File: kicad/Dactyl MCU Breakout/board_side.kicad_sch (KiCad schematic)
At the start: 19 parts, among them J1 Columns, J2 Rows, J3 Thumbs, J4 Display, J5 Split, J6 Extrernal, J7 JST, SW1 Reset, SW2 Battery, SW3 LED, U1 Nice!Nano/2040, U2 74HC595

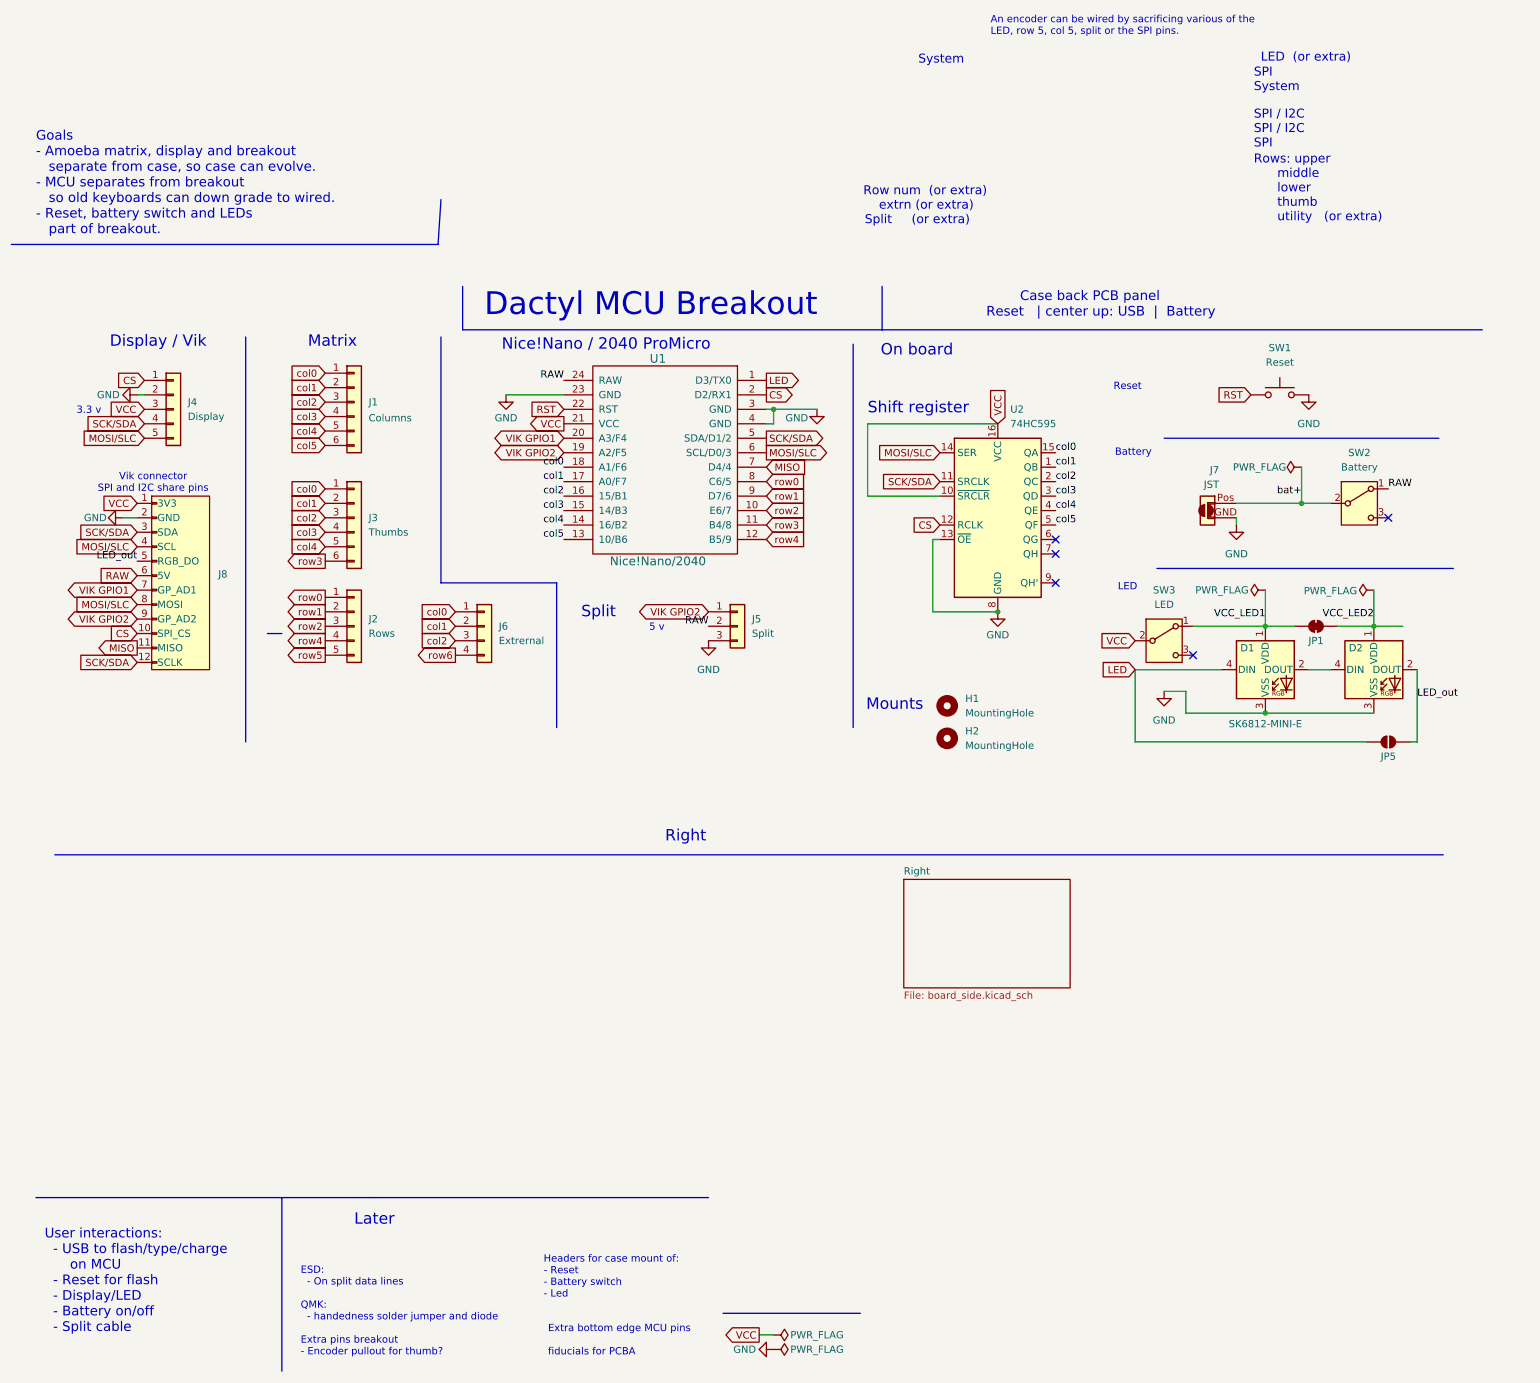
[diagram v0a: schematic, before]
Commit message: refactor: board half sub sheet, some net labels
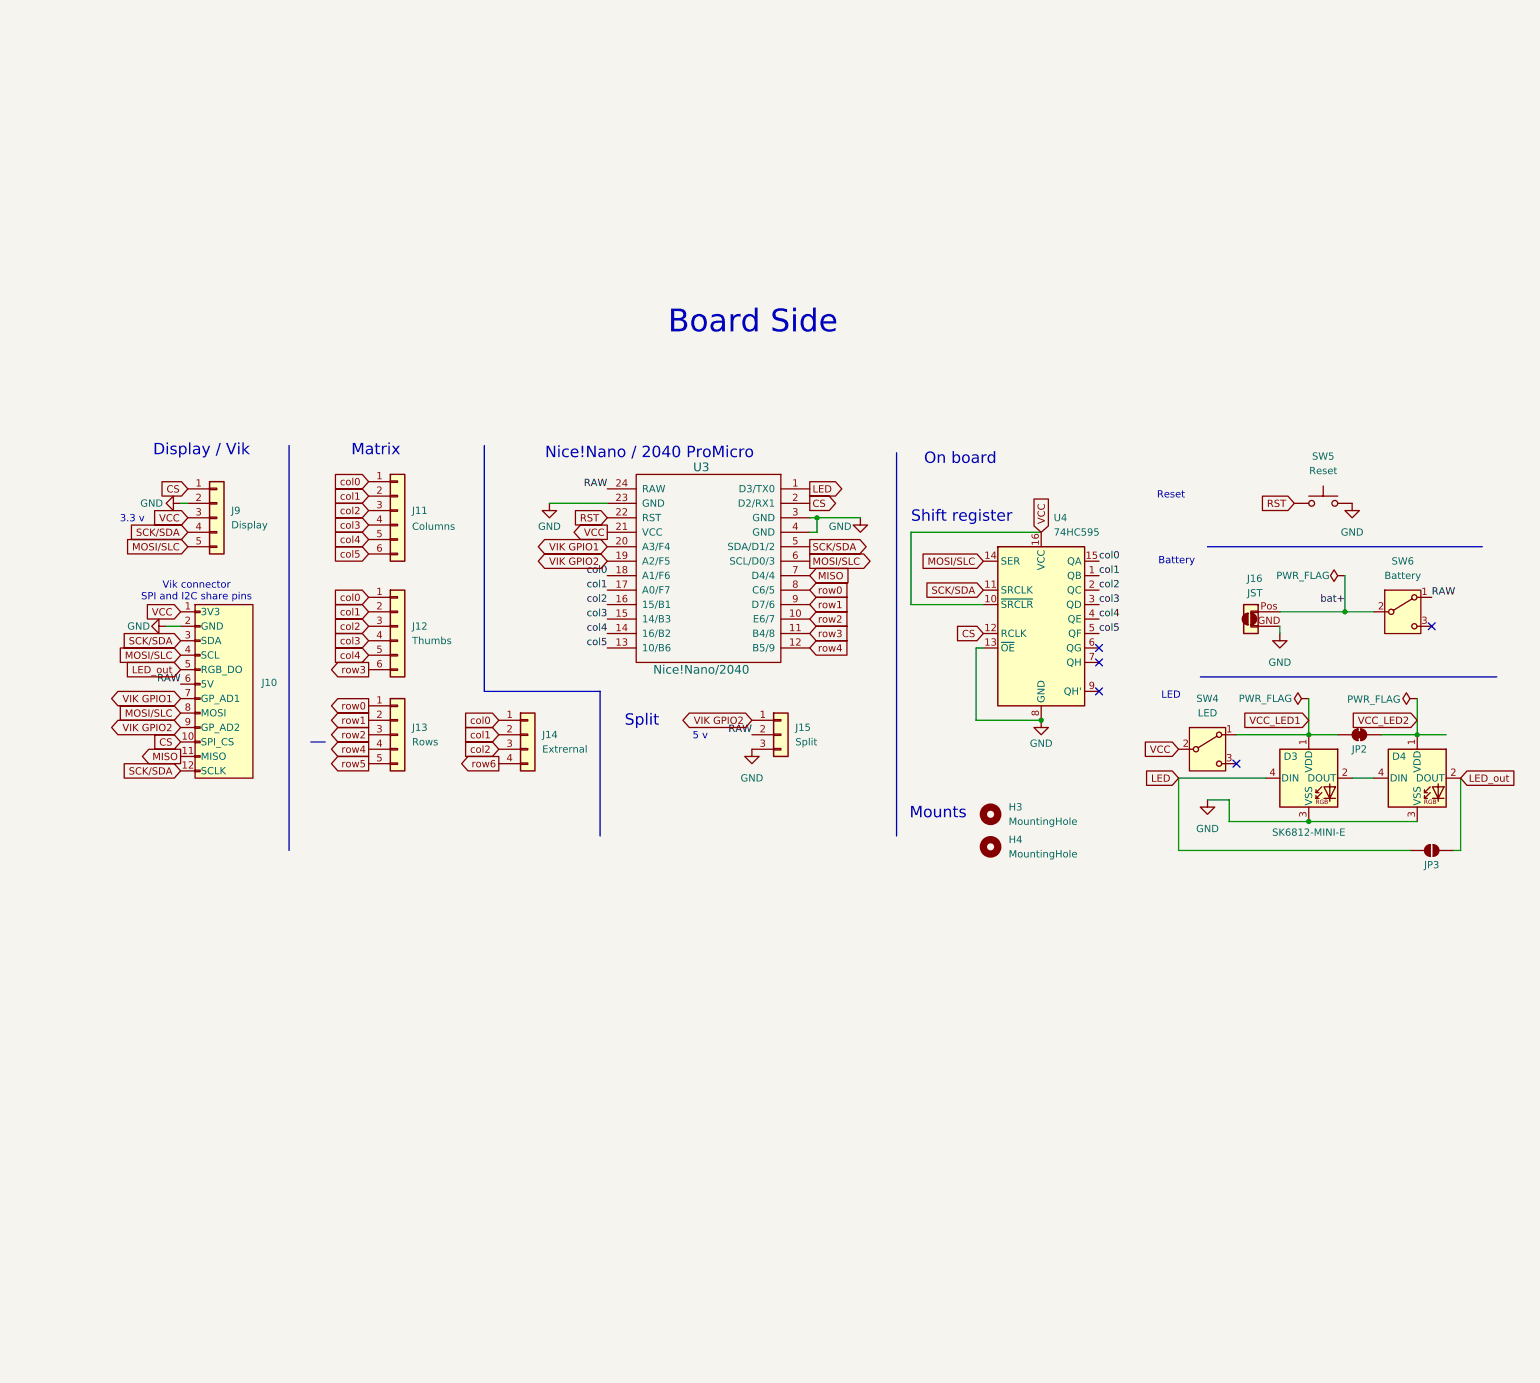
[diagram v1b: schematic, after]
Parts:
- removed D1, D2: SK6812-MINI-E, Dactyl:SK6812-MINI-E-Dog2, symbol Dactyl:SK6812-MINI-E
- removed H1, H2: MountingHole, MountingHole:MountingHole_3.2mm_M3_DIN965_Pad, symbol Mechanical:MountingHole
- removed J1: Columns, Connector_PinHeader_2.54mm:PinHeader_1x06_P2.54mm_Vertical, symbol Connector_Generic:Conn_01x06
- removed J2: Rows, Connector_PinHeader_2.54mm:PinHeader_1x05_P2.54mm_Vertical, symbol Connector_Generic:Conn_01x05
- removed J3: Thumbs, Connector_PinHeader_2.54mm:PinHeader_1x06_P2.54mm_Vertical, symbol Connector_Generic:Conn_01x06
- removed J4: Display, Connector_PinHeader_2.54mm:PinHeader_1x05_P2.54mm_Vertical, symbol Connector_Generic:Conn_01x05
- removed J5: Split, Connector_PinHeader_2.54mm:PinHeader_1x03_P2.54mm_Vertical, symbol Connector_Generic:Conn_01x03
- removed J6: Extrernal, Connector_PinHeader_2.54mm:PinHeader_1x04_P2.54mm_Vertical, symbol Connector_Generic:Conn_01x04
- removed J7: JST, Dactyl:JST_PH_S2B-PH-K_1x02_P2.00mm_Horizontal, symbol Dactyl:Conn_01x02_Jump_Two_Side
- removed J8: ~, symbol Dactyl:vik-keyboard-connector
- removed JP1: LED2 cutoff, Jumper:SolderJumper-2_P1.3mm_Bridged_RoundedPad1.0x1.5mm, symbol Jumper:SolderJumper_2_Bridged
- removed JP5: LED2 cutoff, Jumper:SolderJumper-2_P1.3mm_Bridged_RoundedPad1.0x1.5mm, symbol Jumper:SolderJumper_2_Open
- removed SW1: Reset, Dactyl:SW_Tactile_SKHL_Angled, symbol Switch:SW_Push
- removed SW2: Battery, Dactyl:SW_SPDT_JS202011AQN_wider, symbol Switch:SW_SPDT
- removed SW3: LED, Dactyl:SW_SPDT_JS202011AQN_wider, symbol Switch:SW_SPDT
- removed U1: Nice!Nano/2040, Dactyl:ProMicro_unrouted, symbol Dactyl:ProMicro_r
- removed U2: 74HC595, symbol 74xx:74HC595
- added D3, D4: SK6812-MINI-E, Dactyl:SK6812-MINI-E-Dog2, symbol Dactyl:SK6812-MINI-E
- added H3, H4: MountingHole, MountingHole:MountingHole_3.2mm_M3_DIN965_Pad, symbol Mechanical:MountingHole
- added J10: ~, symbol Dactyl:vik-keyboard-connector
- added J11: Columns, Connector_PinHeader_2.54mm:PinHeader_1x06_P2.54mm_Vertical, symbol Connector_Generic:Conn_01x06
- added J12: Thumbs, Connector_PinHeader_2.54mm:PinHeader_1x06_P2.54mm_Vertical, symbol Connector_Generic:Conn_01x06
- added J13: Rows, Connector_PinHeader_2.54mm:PinHeader_1x05_P2.54mm_Vertical, symbol Connector_Generic:Conn_01x05
- added J14: Extrernal, Connector_PinHeader_2.54mm:PinHeader_1x04_P2.54mm_Vertical, symbol Connector_Generic:Conn_01x04
- added J15: Split, Connector_PinHeader_2.54mm:PinHeader_1x03_P2.54mm_Vertical, symbol Connector_Generic:Conn_01x03
- added J16: JST, Dactyl:JST_PH_S2B-PH-K_1x02_P2.00mm_Horizontal, symbol Dactyl:Conn_01x02_Jump_Two_Side
- added J9: Display, Connector_PinHeader_2.54mm:PinHeader_1x05_P2.54mm_Vertical, symbol Connector_Generic:Conn_01x05
- added JP2: LED2 cutoff, Jumper:SolderJumper-2_P1.3mm_Bridged_RoundedPad1.0x1.5mm, symbol Jumper:SolderJumper_2_Bridged
- added JP3: LED2 cutoff, Jumper:SolderJumper-2_P1.3mm_Bridged_RoundedPad1.0x1.5mm, symbol Jumper:SolderJumper_2_Open
- added SW4: LED, Dactyl:SW_SPDT_JS202011AQN_wider, symbol Switch:SW_SPDT
- added SW5: Reset, Dactyl:SW_Tactile_SKHL_Angled, symbol Switch:SW_Push
- added SW6: Battery, Dactyl:SW_SPDT_JS202011AQN_wider, symbol Switch:SW_SPDT
- added U3: Nice!Nano/2040, Dactyl:ProMicro_unrouted, symbol Dactyl:ProMicro_r
- added U4: 74HC595, symbol 74xx:74HC595
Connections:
- net CS: now also J10.10 (SPI_CS), J9.1 (Pin_1), U3.2 (D2/RX1), U4.12 (RCLK)
- net GND: now also D3.3 (VSS), D4.3 (VSS), J10.2 (GND), J15.3 (Pin_3), J16.GND, J9.2 (Pin_2), SW5.2, U3.23 (GND), U3.3 (GND), U3.4 (GND), U4.13 (~{OE}), U4.8 (GND)
- net LED: now also D3.4 (DIN), JP3.1 (A), U3.1 (D3/TX0)
- net LED_out: now also D4.2 (DOUT), J10.5 (RGB_DO), JP3.2 (B)
- net MISO: now also J10.11 (MISO), U3.7 (D4/4)
- net MOSI/SLC: now also J10.4 (SCL), J10.8 (MOSI), J9.5 (Pin_5), U3.6 (SCL/D0/3), U4.14 (SER)
- net RAW: now also J10.6 (5V), J15.2 (Pin_2), SW6.1 (A), U3.24 (RAW)
- net RST: now also SW5.1, U3.22 (RST)
- net SCK/SDA: now also J10.12 (SCLK), J10.3 (SDA), J9.4 (Pin_4), U3.5 (SDA/D1/2), U4.11 (SRCLK)
- net VCC: now also J10.1 (3V3), J9.3 (Pin_3), SW4.2 (B), U3.21 (VCC), U4.10 (~{SRCLR}), U4.16 (VCC)
- net VCC_LED1: now also D3.1 (VDD), JP2.1 (A), SW4.1 (A)
- net VCC_LED2: now also D4.1 (VDD), JP2.2 (B)
- net VIK GPIO1: now also J10.7 (GP_AD1), U3.20 (A3/F4)
- net VIK GPIO2: now also J10.9 (GP_AD2), J15.1 (Pin_1), U3.19 (A2/F5)
- net bat+: now also J16.Pos, SW6.2 (B)
- net col0: now also J11.1 (Pin_1), J12.1 (Pin_1), J14.1 (Pin_1), U3.18 (A1/F6), U4.15 (QA)
- net col1: now also J11.2 (Pin_2), J12.2 (Pin_2), J14.2 (Pin_2), U3.17 (A0/F7), U4.1 (QB)
- net col2: now also J11.3 (Pin_3), J12.3 (Pin_3), J14.3 (Pin_3), U3.16 (15/B1), U4.2 (QC)
- net col3: now also J11.4 (Pin_4), J12.4 (Pin_4), U3.15 (14/B3), U4.3 (QD)
- net col4: now also J11.5 (Pin_5), J12.5 (Pin_5), U3.14 (16/B2), U4.4 (QE)
- net col5: now also J11.6 (Pin_6), U3.13 (10/B6), U4.5 (QF)
- net row0: now also J13.1 (Pin_1), U3.8 (C6/5)
- net row1: now also J13.2 (Pin_2), U3.9 (D7/6)
- net row2: now also J13.3 (Pin_3), U3.10 (E6/7)
- net row3: now also J12.6 (Pin_6), U3.11 (B4/8)
- net row4: now also J13.4 (Pin_4), U3.12 (B5/9)
- net row5: now also J13.5 (Pin_5)
- net row6: now also J14.4 (Pin_4)
- new net: D3.2 (DOUT), D4.4 (DIN)
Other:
- removed sheet Right
- note added: "Board Side"
- note removed: "${TITLE}"
- note removed: "An encoder can be wired by sacrificing various of the LED, row 5, col 5, split or the SPI pins."
- note removed: "Case back PCB panel Reset | center up: USB | Battery"
- note removed: "ESD: - On split data lines QMK: - handedness solder jumper and diode Extra pins breakout - Encoder pullout for thumb?"
- note removed: "Extra bottom edge MCU pins fiducials for PCBA"
- note removed: "Goals - Amoeba matrix, display and breakout separate from case, so case can evolve. - MCU separates from breakout so old keyboards can down grade to wired. - Reset, battery switch and LEDs part of breakout."
- note removed: "Headers for case mount of: - Reset - Battery switch - Led"
- note removed: "LED (or extra)"
- note removed: "Later"
- note removed: "Right"
- note removed: "Row num (or extra) extrn (or extra)"
- note removed: "Rows: upper middle lower thumb utility (or extra)"
- note removed: "SPI"
- note removed: "SPI / I2C SPI / I2C SPI"
- note removed: "Split (or extra)"
- note removed: "System"
- note removed: "User interactions: - USB to flash/type/charge on MCU - Reset for flash - Display/LED - Battery on/off - Split cable"
- title: Dactyl MCU Breakout -> (none)
